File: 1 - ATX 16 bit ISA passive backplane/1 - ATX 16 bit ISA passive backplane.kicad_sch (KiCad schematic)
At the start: 22 parts, among them J1 BUS 1, J10 AB15, J11 AB15, J12 AB15, J13 AB15, J14 AB15, J15 AB15, J16 AB15, J2 BUS 2, J3 BUS 3, J4 BUS 4, J5 BUS 5, J6 BUS 6, J7 BUS 7, J8 BREADBOARD HEADER (RC2014 COM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, J9 EXTENDED HEADER

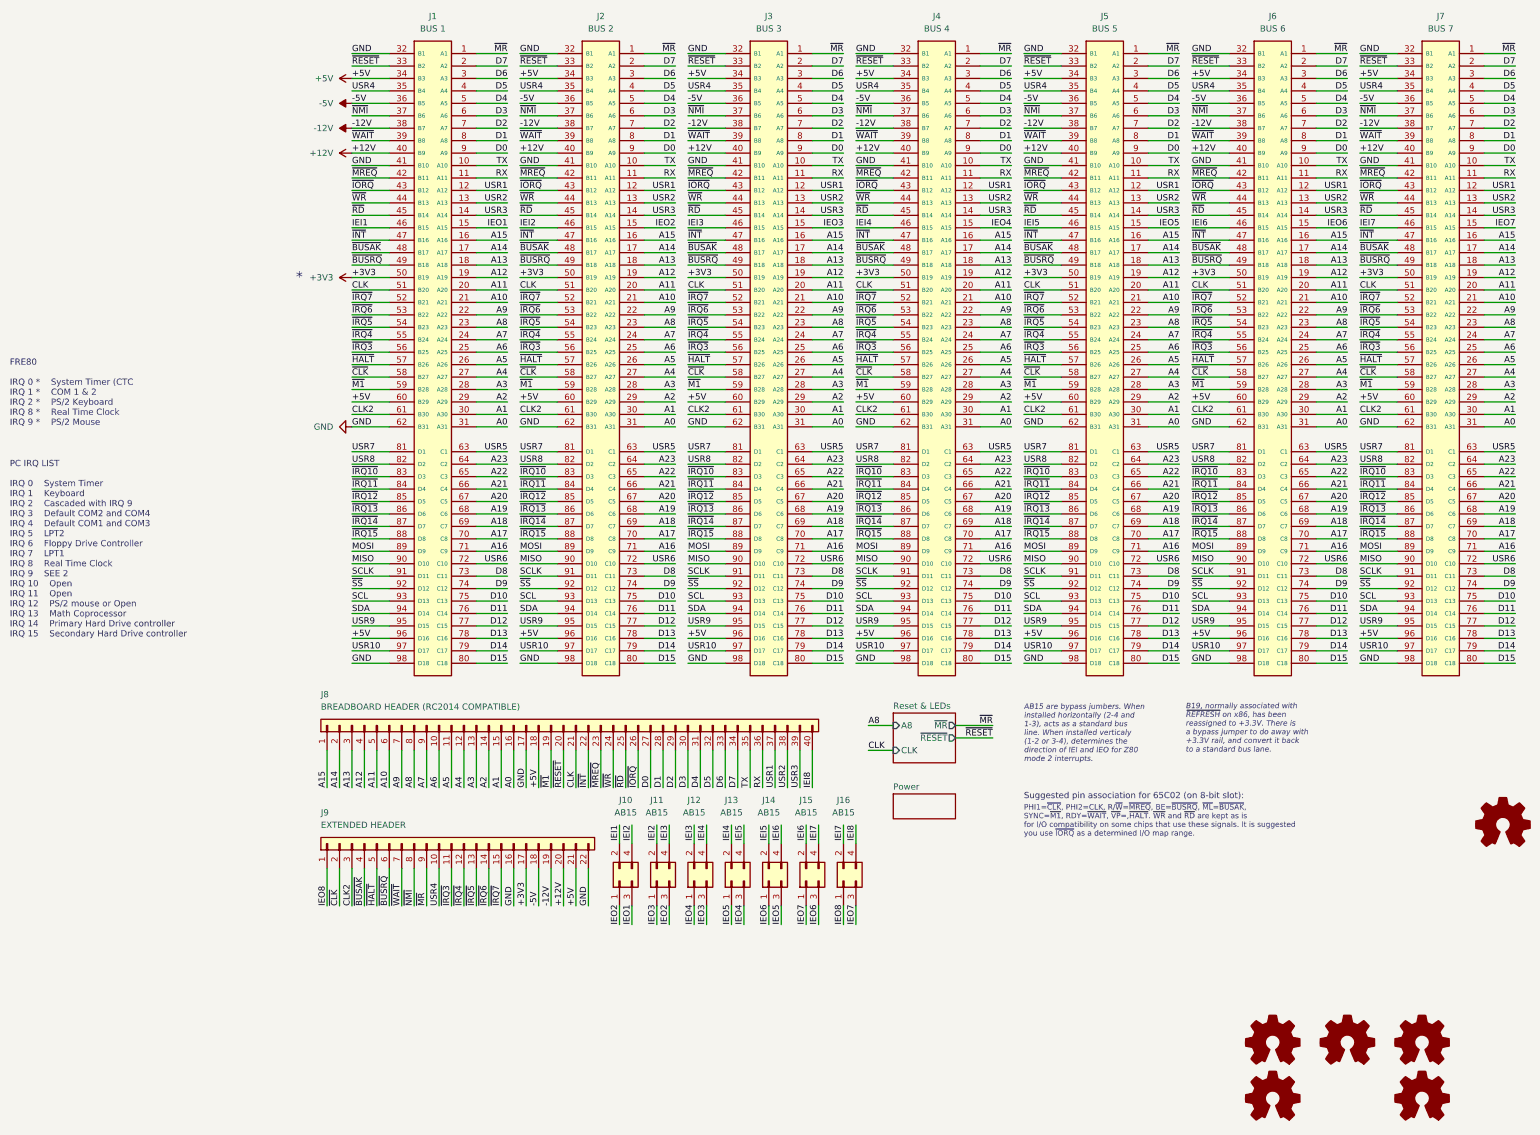
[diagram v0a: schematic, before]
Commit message: Removed unessential components and added capacitors on the bus lanes. Still need work for on the silkscreen side.
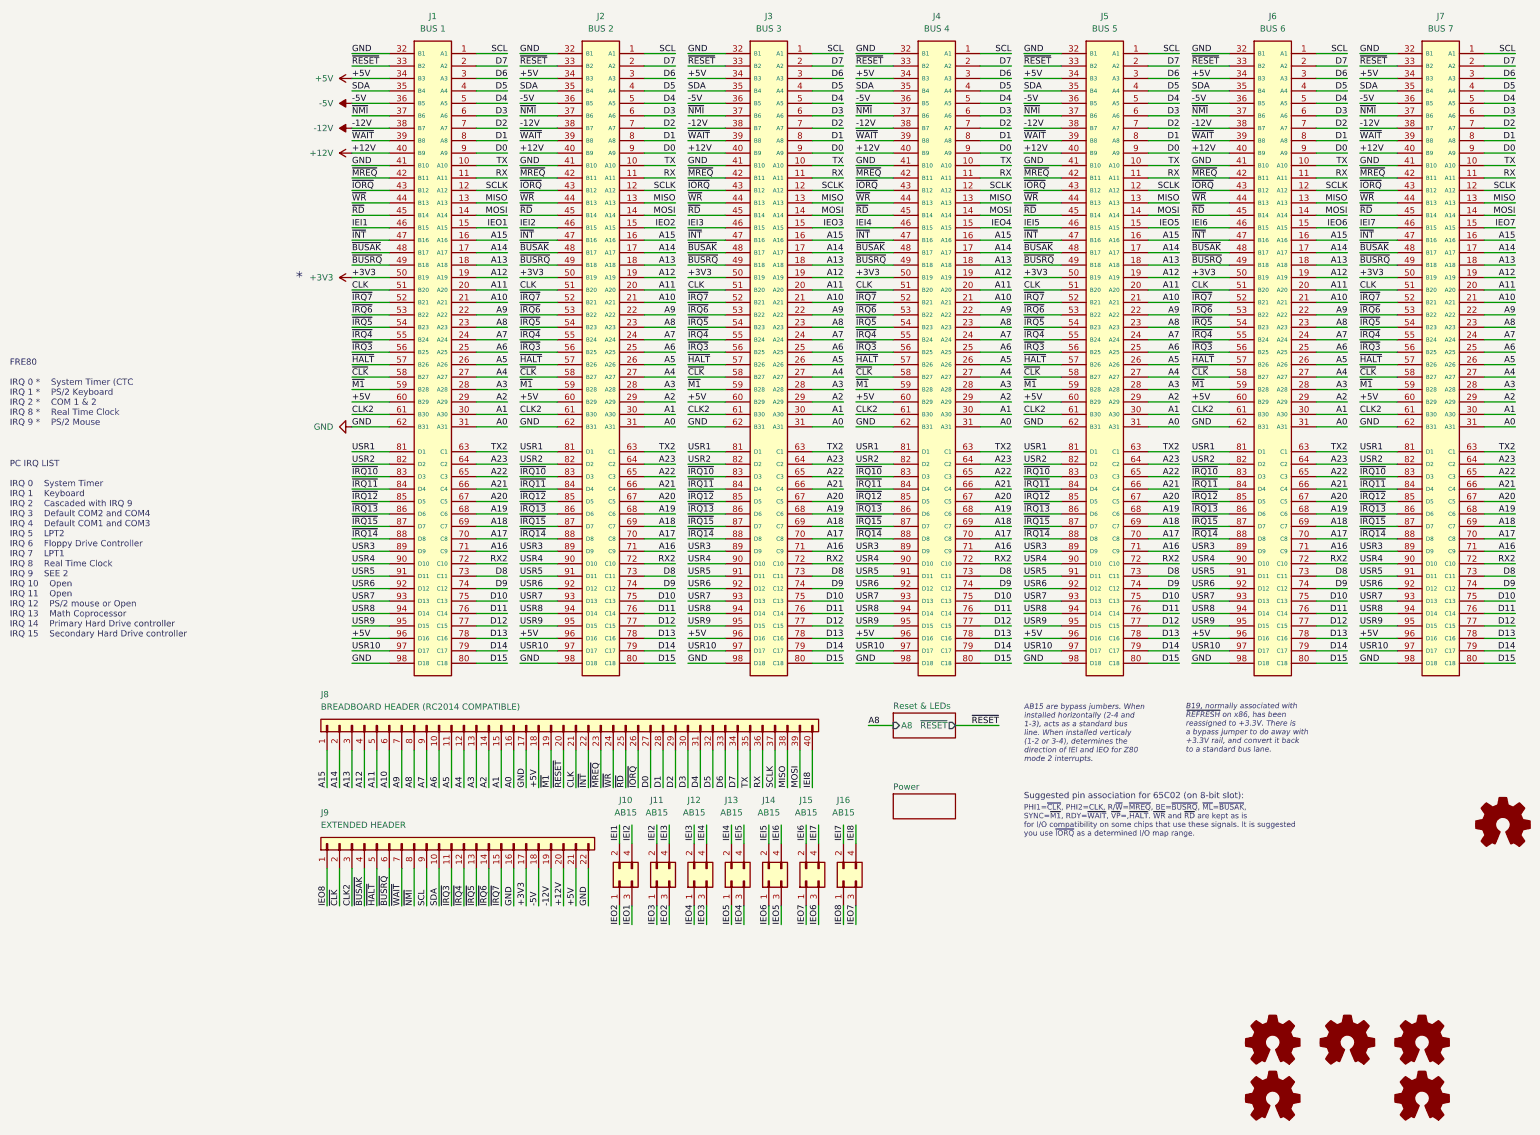
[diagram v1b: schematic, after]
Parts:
- J10, J11, J12, J13, J14, J15, J16: footprint 0 - Library:PinHeader_2x02_Vertical -> 0 - Library:PinHeader_2x2_Vertical (Modified)
- renumbered LOGO2 to LOGO1, LOGO1 to LOGO2, LOGO7 to LOGO5, LOGO5 to LOGO6
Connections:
- net ~{MR} is gone; now on net SCL: J1.1 (A1), J2.1 (A1), J3.1 (A1), J4.1 (A1), J5.1 (A1), J6.1 (A1), J7.1 (A1), J9.9 (Pin_9)
- net ~{SS} is gone; now on net USR6: J1.92 (D12), J2.92 (D12), J3.92 (D12), J4.92 (D12), J5.92 (D12), J6.92 (D12), J7.92 (D12)
- net MISO: now also J1.13 (A13), J2.13 (A13), J3.13 (A13), J4.13 (A13), J5.13 (A13), J6.13 (A13), J7.13 (A13), J8.38 (Pin_38); no longer J1.90 (D10), J2.90 (D10), J3.90 (D10), J4.90 (D10), J5.90 (D10), J6.90 (D10), J7.90 (D10)
- net MOSI: now also J1.14 (A14), J2.14 (A14), J3.14 (A14), J4.14 (A14), J5.14 (A14), J6.14 (A14), J7.14 (A14), J8.39 (Pin_39); no longer J1.89 (D9), J2.89 (D9), J3.89 (D9), J4.89 (D9), J5.89 (D9), J6.89 (D9), J7.89 (D9)
- net SCL: no longer J1.93 (D13), J2.93 (D13), J3.93 (D13), J4.93 (D13), J5.93 (D13), J6.93 (D13), J7.93 (D13)
- net SCLK: now also J1.12 (A12), J2.12 (A12), J3.12 (A12), J4.12 (A12), J5.12 (A12), J6.12 (A12), J7.12 (A12), J8.37 (Pin_37); no longer J1.91 (D11), J2.91 (D11), J3.91 (D11), J4.91 (D11), J5.91 (D11), J6.91 (D11), J7.91 (D11)
- net SDA: now also J1.35 (B4), J2.35 (B4), J3.35 (B4), J4.35 (B4), J5.35 (B4), J6.35 (B4), J7.35 (B4), J9.10 (Pin_10); no longer J1.94 (D14), J2.94 (D14), J3.94 (D14), J4.94 (D14), J5.94 (D14), J6.94 (D14), J7.94 (D14)
- net USR1: now also J1.81 (D1), J2.81 (D1), J3.81 (D1), J4.81 (D1), J5.81 (D1), J6.81 (D1), J7.81 (D1); no longer J1.12 (A12), J2.12 (A12), J3.12 (A12), J4.12 (A12), J5.12 (A12), J6.12 (A12), J7.12 (A12), J8.37 (Pin_37)
- net USR2: now also J1.82 (D2), J2.82 (D2), J3.82 (D2), J4.82 (D2), J5.82 (D2), J6.82 (D2), J7.82 (D2); no longer J1.13 (A13), J2.13 (A13), J3.13 (A13), J4.13 (A13), J5.13 (A13), J6.13 (A13), J7.13 (A13), J8.38 (Pin_38)
- net USR3: now also J1.89 (D9), J2.89 (D9), J3.89 (D9), J4.89 (D9), J5.89 (D9), J6.89 (D9), J7.89 (D9); no longer J1.14 (A14), J2.14 (A14), J3.14 (A14), J4.14 (A14), J5.14 (A14), J6.14 (A14), J7.14 (A14), J8.39 (Pin_39)
- net USR4: now also J1.90 (D10), J2.90 (D10), J3.90 (D10), J4.90 (D10), J5.90 (D10), J6.90 (D10), J7.90 (D10); no longer J1.35 (B4), J2.35 (B4), J3.35 (B4), J4.35 (B4), J5.35 (B4), J6.35 (B4), J7.35 (B4), J9.10 (Pin_10)
- net USR5: now also J1.91 (D11), J2.91 (D11), J3.91 (D11), J4.91 (D11), J5.91 (D11), J6.91 (D11), J7.91 (D11); no longer J1.63 (C1), J2.63 (C1), J3.63 (C1), J4.63 (C1), J5.63 (C1), J6.63 (C1), J7.63 (C1)
- net USR6: no longer J1.72 (C10), J2.72 (C10), J3.72 (C10), J4.72 (C10), J5.72 (C10), J6.72 (C10), J7.72 (C10)
- net USR7: now also J1.93 (D13), J2.93 (D13), J3.93 (D13), J4.93 (D13), J5.93 (D13), J6.93 (D13), J7.93 (D13); no longer J1.81 (D1), J2.81 (D1), J3.81 (D1), J4.81 (D1), J5.81 (D1), J6.81 (D1), J7.81 (D1)
- net USR8: now also J1.94 (D14), J2.94 (D14), J3.94 (D14), J4.94 (D14), J5.94 (D14), J6.94 (D14), J7.94 (D14); no longer J1.82 (D2), J2.82 (D2), J3.82 (D2), J4.82 (D2), J5.82 (D2), J6.82 (D2), J7.82 (D2)
- net ~{IRQ14}: now also J1.88 (D8), J2.88 (D8), J3.88 (D8), J4.88 (D8), J5.88 (D8), J6.88 (D8), J7.88 (D8); no longer J1.87 (D7), J2.87 (D7), J3.87 (D7), J4.87 (D7), J5.87 (D7), J6.87 (D7), J7.87 (D7)
- net ~{IRQ15}: now also J1.87 (D7), J2.87 (D7), J3.87 (D7), J4.87 (D7), J5.87 (D7), J6.87 (D7), J7.87 (D7); no longer J1.88 (D8), J2.88 (D8), J3.88 (D8), J4.88 (D8), J5.88 (D8), J6.88 (D8), J7.88 (D8)
- new net RX2: J1.72 (C10), J2.72 (C10), J3.72 (C10), J4.72 (C10), J5.72 (C10), J6.72 (C10), J7.72 (C10)
- new net TX2: J1.63 (C1), J2.63 (C1), J3.63 (C1), J4.63 (C1), J5.63 (C1), J6.63 (C1), J7.63 (C1)
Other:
- sheet Reset & LEDs ports: added none; removed CLK, ~{MR}
- note added: "FRE80 IRQ 0 * System Timer (CTC IRQ 1 * PS/2 Keyboard IRQ 2 * COM 1 & 2 IRQ 8 * Real Time Clock IRQ 9 * PS/2 Mouse"
- note removed: "FRE80 IRQ 0 * System Timer (CTC IRQ 1 * COM 1 & 2 IRQ 2 * PS/2 Keyboard IRQ 8 * Real Time Clock IRQ 9 * PS/2 Mouse"

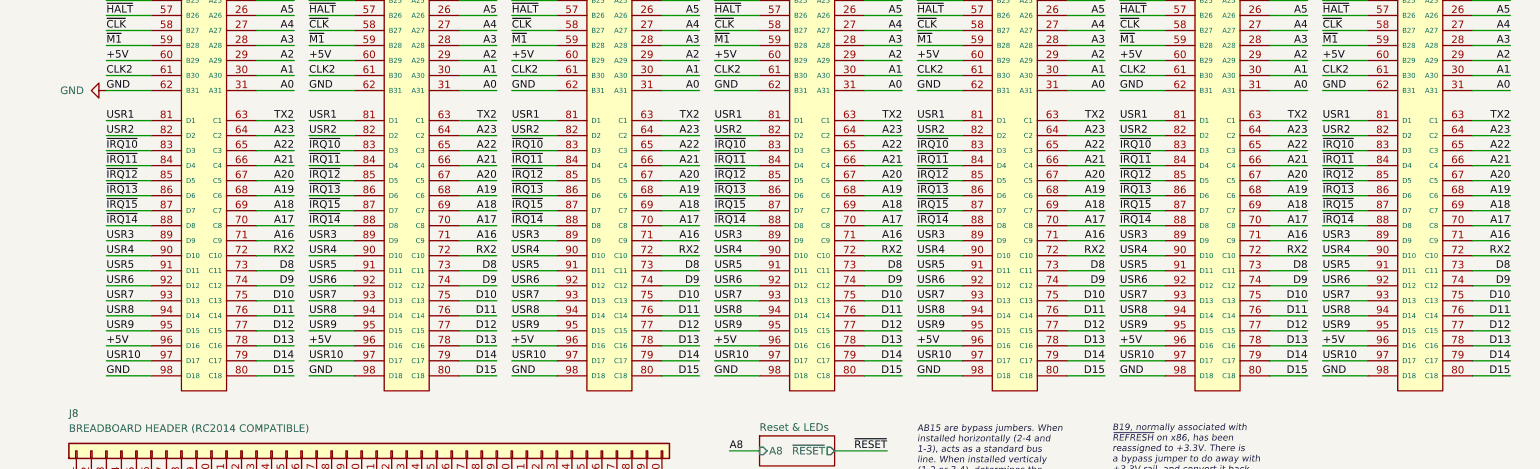
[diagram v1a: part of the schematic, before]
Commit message: Minor tweaks to the backplane, and will be sending it out for manufacture
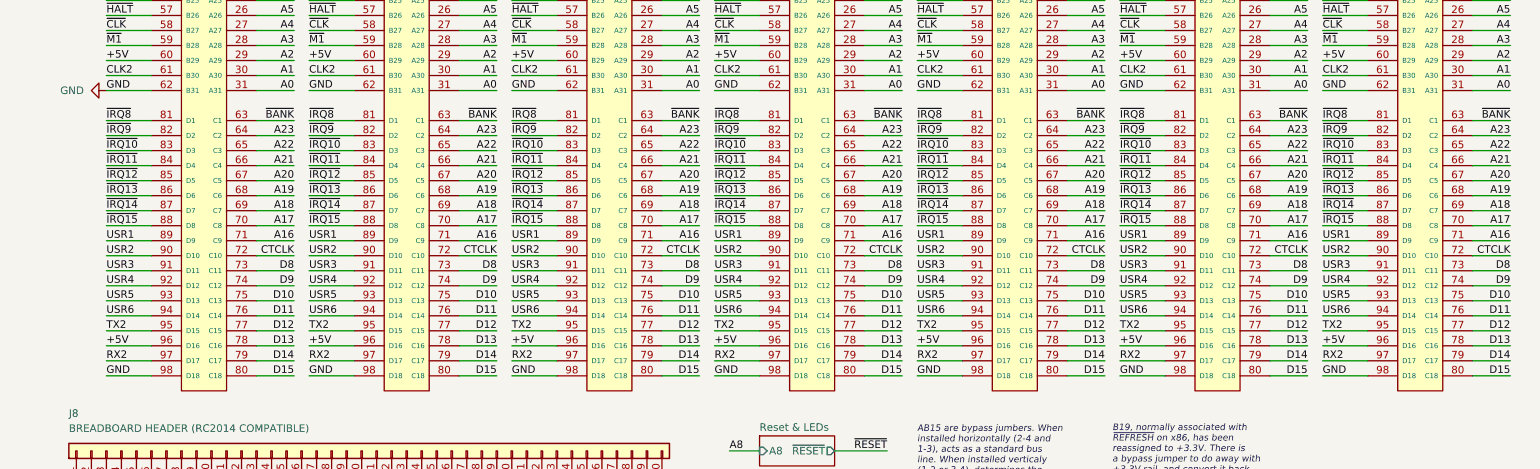
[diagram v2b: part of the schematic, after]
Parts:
- J1, J2, J3, J4, J5, J6, J7: footprint 0 - Library:ISA_Connector_98 -> 0_Library:ISA_Connector_98
- J10, J11, J12, J13, J14, J15, J16: footprint 0 - Library:PinHeader_2x2_Vertical (Modified) -> 0_Library:PinHeader_2x2_Vertical (Modified)
- LOGO1: footprint 0 - Library:MicroHobbyist -> 0_Library:MicroHobbyist
- LOGO3: footprint 0 - Library:JLCPCB Logo 3 -> 0_Library:JLCPCB Logo 3
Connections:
- net USR10 is gone; now on net RX2: J1.97 (D17), J2.97 (D17), J3.97 (D17), J4.97 (D17), J5.97 (D17), J6.97 (D17), J7.97 (D17)
- net USR7 is gone; now on net USR5: J1.93 (D13), J2.93 (D13), J3.93 (D13), J4.93 (D13), J5.93 (D13), J6.93 (D13), J7.93 (D13)
- net USR8 is gone; now on net USR6: J1.94 (D14), J2.94 (D14), J3.94 (D14), J4.94 (D14), J5.94 (D14), J6.94 (D14), J7.94 (D14)
- net USR9 is gone; now on net TX2: J1.95 (D15), J2.95 (D15), J3.95 (D15), J4.95 (D15), J5.95 (D15), J6.95 (D15), J7.95 (D15)
- net RX2: no longer J1.72 (C10), J2.72 (C10), J3.72 (C10), J4.72 (C10), J5.72 (C10), J6.72 (C10), J7.72 (C10)
- net TX2: no longer J1.63 (C1), J2.63 (C1), J3.63 (C1), J4.63 (C1), J5.63 (C1), J6.63 (C1), J7.63 (C1)
- net USR1: now also J1.89 (D9), J2.89 (D9), J3.89 (D9), J4.89 (D9), J5.89 (D9), J6.89 (D9), J7.89 (D9); no longer J1.81 (D1), J2.81 (D1), J3.81 (D1), J4.81 (D1), J5.81 (D1), J6.81 (D1), J7.81 (D1)
- net USR2: now also J1.90 (D10), J2.90 (D10), J3.90 (D10), J4.90 (D10), J5.90 (D10), J6.90 (D10), J7.90 (D10); no longer J1.82 (D2), J2.82 (D2), J3.82 (D2), J4.82 (D2), J5.82 (D2), J6.82 (D2), J7.82 (D2)
- net USR3: now also J1.91 (D11), J2.91 (D11), J3.91 (D11), J4.91 (D11), J5.91 (D11), J6.91 (D11), J7.91 (D11); no longer J1.89 (D9), J2.89 (D9), J3.89 (D9), J4.89 (D9), J5.89 (D9), J6.89 (D9), J7.89 (D9)
- net USR4: now also J1.92 (D12), J2.92 (D12), J3.92 (D12), J4.92 (D12), J5.92 (D12), J6.92 (D12), J7.92 (D12); no longer J1.90 (D10), J2.90 (D10), J3.90 (D10), J4.90 (D10), J5.90 (D10), J6.90 (D10), J7.90 (D10)
- net USR5: no longer J1.91 (D11), J2.91 (D11), J3.91 (D11), J4.91 (D11), J5.91 (D11), J6.91 (D11), J7.91 (D11)
- net USR6: no longer J1.92 (D12), J2.92 (D12), J3.92 (D12), J4.92 (D12), J5.92 (D12), J6.92 (D12), J7.92 (D12)
- net ~{IRQ14}: now also J1.87 (D7), J2.87 (D7), J3.87 (D7), J4.87 (D7), J5.87 (D7), J6.87 (D7), J7.87 (D7); no longer J1.88 (D8), J2.88 (D8), J3.88 (D8), J4.88 (D8), J5.88 (D8), J6.88 (D8), J7.88 (D8)
- net ~{IRQ15}: now also J1.88 (D8), J2.88 (D8), J3.88 (D8), J4.88 (D8), J5.88 (D8), J6.88 (D8), J7.88 (D8); no longer J1.87 (D7), J2.87 (D7), J3.87 (D7), J4.87 (D7), J5.87 (D7), J6.87 (D7), J7.87 (D7)
- new net CTCLK: J1.72 (C10), J2.72 (C10), J3.72 (C10), J4.72 (C10), J5.72 (C10), J6.72 (C10), J7.72 (C10)
- new net ~{BANK}: J1.63 (C1), J2.63 (C1), J3.63 (C1), J4.63 (C1), J5.63 (C1), J6.63 (C1), J7.63 (C1)
- new net ~{IRQ8}: J1.81 (D1), J2.81 (D1), J3.81 (D1), J4.81 (D1), J5.81 (D1), J6.81 (D1), J7.81 (D1)
- new net ~{IRQ9}: J1.82 (D2), J2.82 (D2), J3.82 (D2), J4.82 (D2), J5.82 (D2), J6.82 (D2), J7.82 (D2)

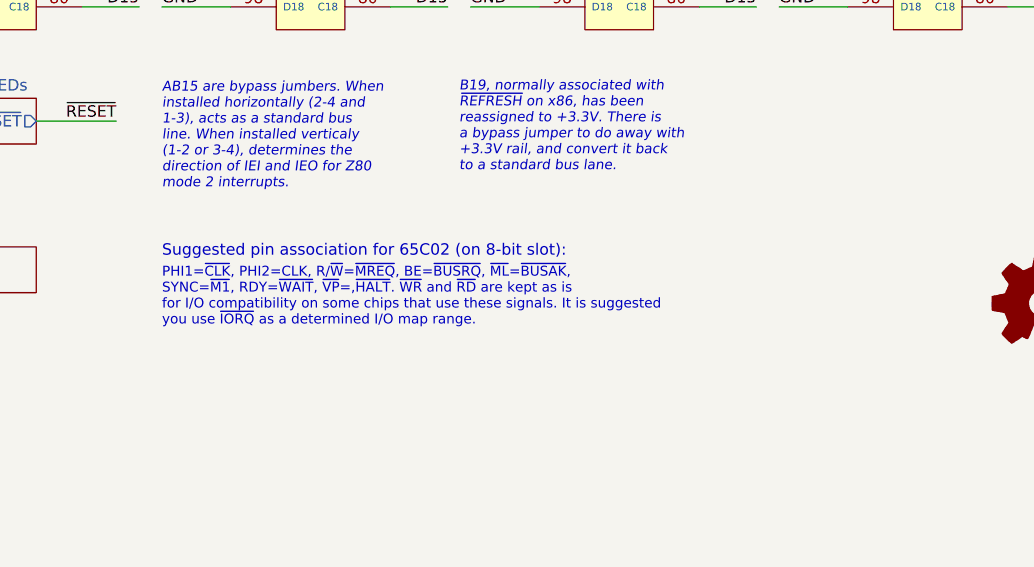
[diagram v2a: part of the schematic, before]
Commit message: Updated disk activity circuit in mother board, and improved layout in CPU card
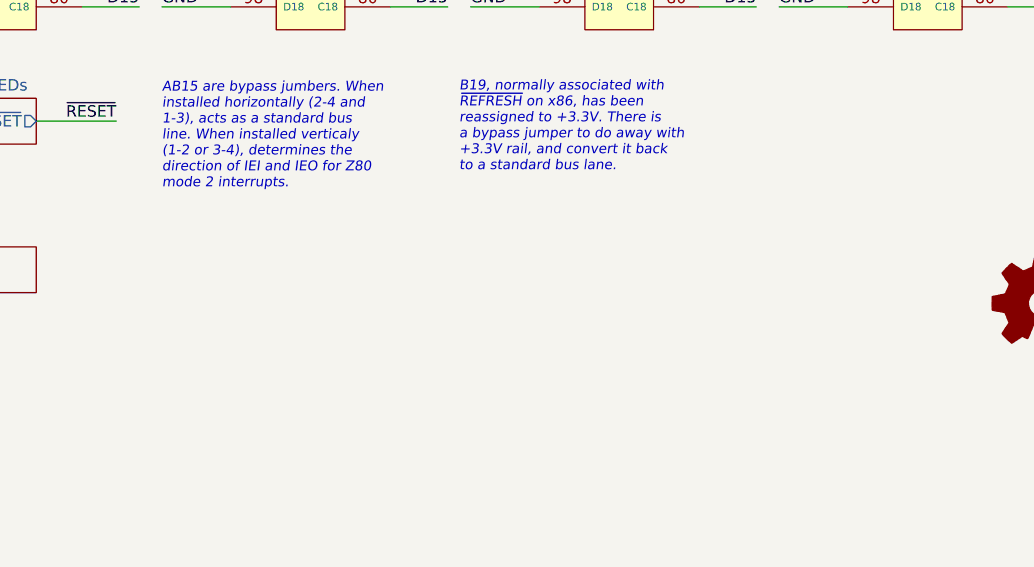
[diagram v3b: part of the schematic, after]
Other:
- note removed: "PHI1=~{CLK}, PHI2=CLK, R/~{W}=~{MREQ}, BE=~{BUSRQ}, ~{ML}=~{BUSAK}, SYNC=~{M1}, RDY=~{WAIT}, ~{VP}=,~{HALT}. ~{WR} and ~{RD} are kept as is for I/O compatibility on some chips that use these signals. It is suggested you use ~{IORQ} as a determined I/O map range."
- note removed: "Suggested pin association for 65C02 (on 8-bit slot):"
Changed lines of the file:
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@@
   (title_block
     (title "7-slot 16-bit ATX backblane with breadboard connectivity")
-    (date "2023-08-12")
+    (date "2023-08-21")
     (rev "2.1")
     (company "Frederic Segard  (@microhobbyist)")
@@
     (stroke (width 0) (type default))
   )
-  (text "Suggested pin association for 65C02 (on 8-bit slot):"
-    (at 161.29 175.26 0)
-    (effects (font (size 1.27 1.27)) (justify left bottom))
-  )
-  (text "PHI1=~{CLK}, PHI2=CLK, R/~{W}=~{MREQ}, BE=~{BUSRQ}, ~{ML}=~{BUSAK},\nSYNC=~{M1}, RDY=~{WAIT}, ~{VP}=,~{HALT}. ~{WR} and ~{RD} are kept as is\nfor I/O compatibility on some chips that use these signals. It is suggested\nyou use ~{IORQ} as a determined I/O map range.\n"
-    (at 161.29 182.88 0)
-    (effects (font (size 1.1 1.1)) (justify left bottom))
-  )
   (text "AB15 are bypass jumbers. When\ninstalled horizontally (2-4 and\n1-3), acts as a standard bus\nline. When installed verticaly\n(1-2 or 3-4), determines the\ndirection of IEI and IEO for Z80\nmode 2 interrupts."

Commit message: Trying to hash out the flaws
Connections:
- net CTCLK is gone; now on net RX2: J1.72 (C10), J2.72 (C10), J3.72 (C10), J4.72 (C10), J5.72 (C10), J6.72 (C10), J7.72 (C10)
- net ~{BANK} is gone; now on net TX2: J1.63 (C1), J2.63 (C1), J3.63 (C1), J4.63 (C1), J5.63 (C1), J6.63 (C1), J7.63 (C1)
- net RX2: no longer J1.97 (D17), J2.97 (D17), J3.97 (D17), J4.97 (D17), J5.97 (D17), J6.97 (D17), J7.97 (D17)
- net TX2: no longer J1.95 (D15), J2.95 (D15), J3.95 (D15), J4.95 (D15), J5.95 (D15), J6.95 (D15), J7.95 (D15)
- new net USR7: J1.95 (D15), J2.95 (D15), J3.95 (D15), J4.95 (D15), J5.95 (D15), J6.95 (D15), J7.95 (D15)
- new net USR8: J1.97 (D17), J2.97 (D17), J3.97 (D17), J4.97 (D17), J5.97 (D17), J6.97 (D17), J7.97 (D17)
